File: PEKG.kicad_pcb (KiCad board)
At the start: 2 copper layers, 90 x 45 mm, 78 parts, among them J1 USB_C_Receptacle, J2 AudioJack3, U10 74LVC1G125, U11 74LVC1G125, U12 NCS21802DMR2G, U13 NCS21802DMR2G, U14 NCS21802DMR2G, U5 TS5A63157DBV, U6 TS5A63157DBV, U7 TS5A63157DBV, U8 NCS21802DMR2G, U9 74LVC1G125

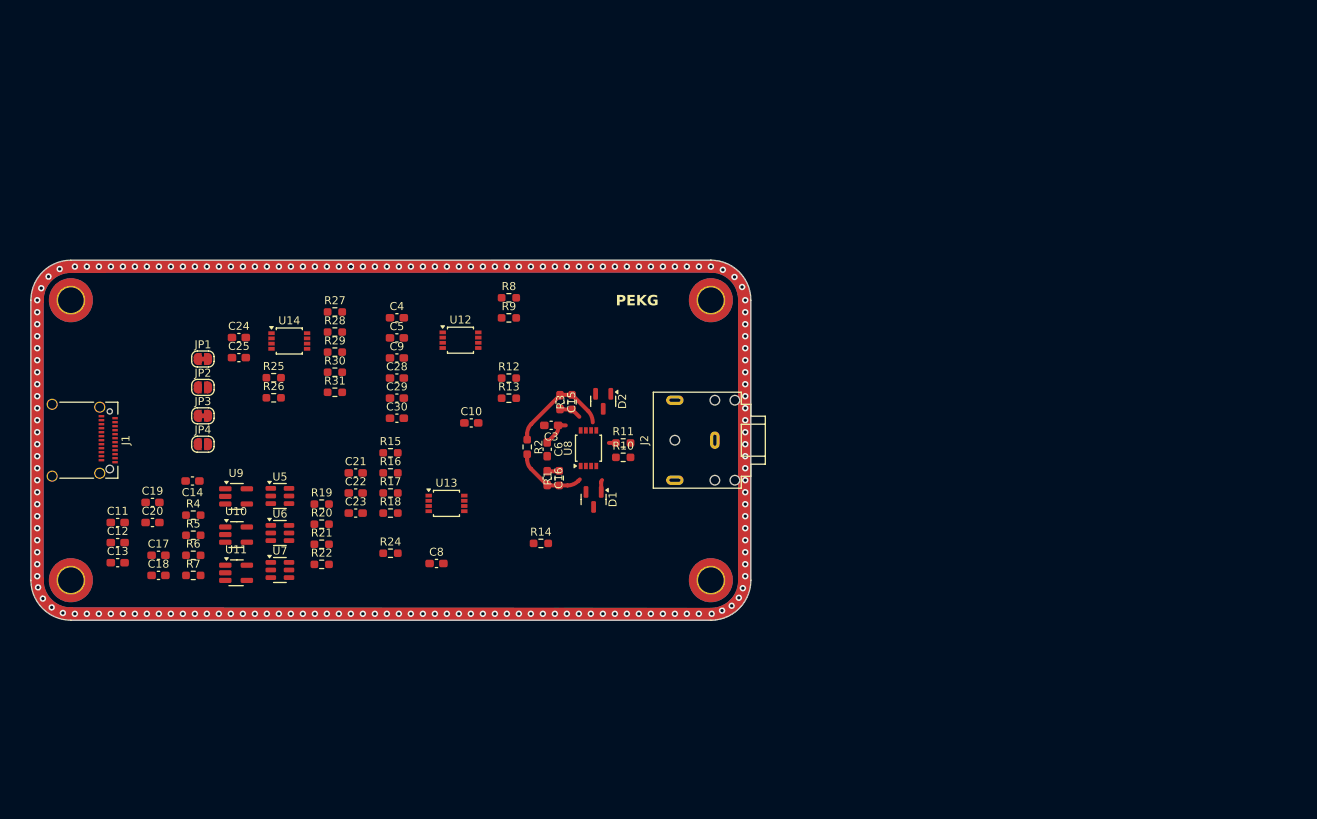
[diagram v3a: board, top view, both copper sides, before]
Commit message: Most all commonents linked to LCSC.
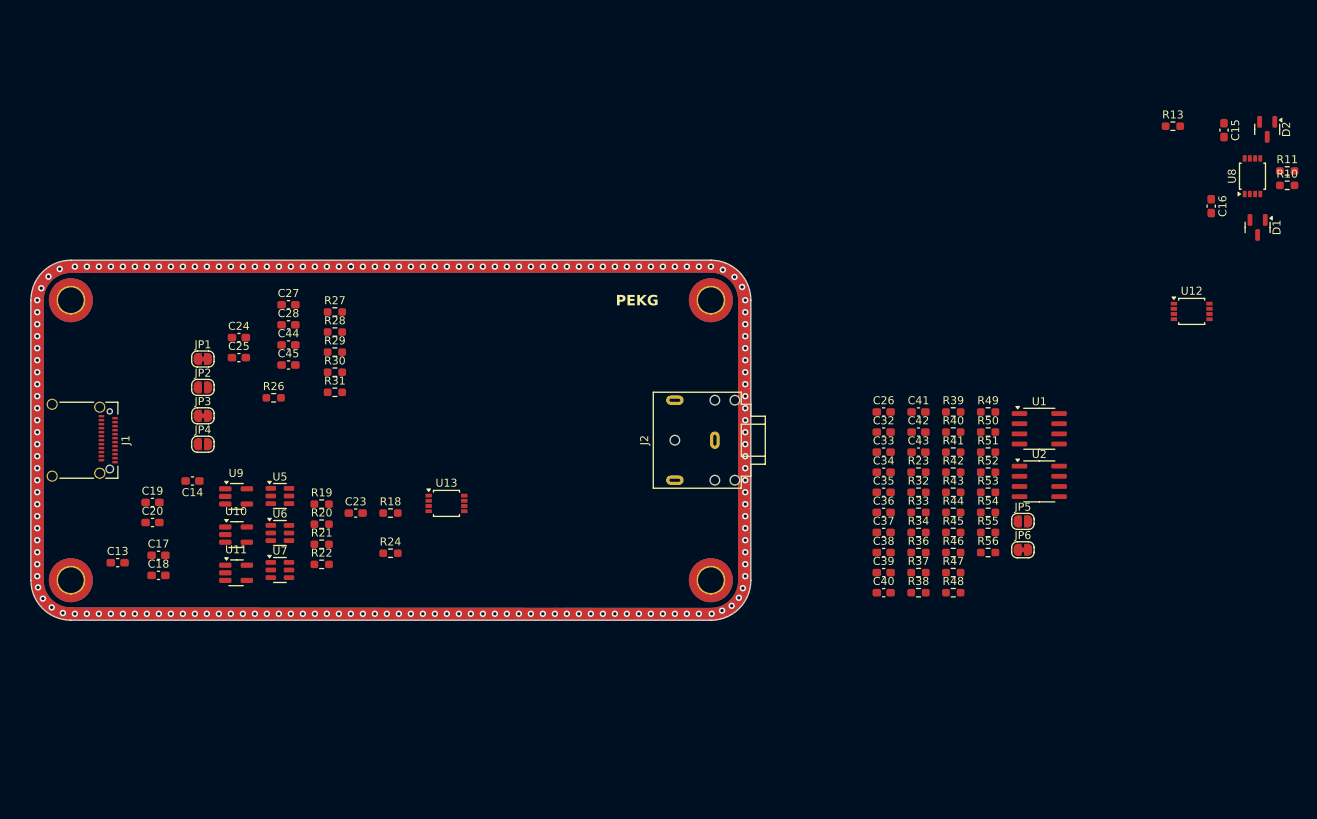
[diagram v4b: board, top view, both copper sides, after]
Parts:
- removed C10, C30, C6, C9: 1u, Capacitor_SMD:C_0603_1608Metric_Pad1.08x0.95mm_HandSolder
- removed C11, C12, C3, C4, C5, C8: 100n, Capacitor_SMD:C_0603_1608Metric_Pad1.08x0.95mm_HandSolder
- removed C21, C22: 10u, Capacitor_SMD:C_0603_1608Metric_Pad1.08x0.95mm_HandSolder
- removed C29: 10n, Capacitor_SMD:C_0603_1608Metric_Pad1.08x0.95mm_HandSolder
- removed R1, R3: 20k, Resistor_SMD:R_0603_1608Metric_Pad0.98x0.95mm_HandSolder
- removed R12, R4, R5, R6, R7: 1k, Resistor_SMD:R_0603_1608Metric_Pad0.98x0.95mm_HandSolder
- removed R14, R15, R16, R17, R25, R8, R9: 100k, Resistor_SMD:R_0603_1608Metric_Pad0.98x0.95mm_HandSolder
- removed R2: 10k, Resistor_SMD:R_0603_1608Metric_Pad0.98x0.95mm_HandSolder
- removed U14: NCS21802DMR2G, Package_SO:OnSemi_Micro8
- added C26: 10u, Capacitor_SMD:C_0603_1608Metric_Pad1.08x0.95mm_HandSolder, F.Cu at (206.6, 119.0)
- added C27: 10u, Capacitor_SMD:C_0603_1608Metric_Pad1.08x0.95mm_HandSolder, F.Cu at (132.2, 105.6)
- added C32: 100n, Capacitor_SMD:C_0603_1608Metric_Pad1.08x0.95mm_HandSolder, F.Cu at (206.6, 121.5)
- added C33: 100n, Capacitor_SMD:C_0603_1608Metric_Pad1.08x0.95mm_HandSolder, F.Cu at (206.6, 124.0)
- added C34: 100n, Capacitor_SMD:C_0603_1608Metric_Pad1.08x0.95mm_HandSolder, F.Cu at (206.6, 126.5)
- added C35: 100n, Capacitor_SMD:C_0603_1608Metric_Pad1.08x0.95mm_HandSolder, F.Cu at (206.6, 129.0)
- added C36: 100n, Capacitor_SMD:C_0603_1608Metric_Pad1.08x0.95mm_HandSolder, F.Cu at (206.6, 131.5)
- added C37: 100n, Capacitor_SMD:C_0603_1608Metric_Pad1.08x0.95mm_HandSolder, F.Cu at (206.6, 134.0)
- added C38: 100n, Capacitor_SMD:C_0603_1608Metric_Pad1.08x0.95mm_HandSolder, F.Cu at (206.6, 136.5)
- added C39: 100n, Capacitor_SMD:C_0603_1608Metric_Pad1.08x0.95mm_HandSolder, F.Cu at (206.6, 139.1)
- added C40: 100n, Capacitor_SMD:C_0603_1608Metric_Pad1.08x0.95mm_HandSolder, F.Cu at (206.6, 141.6)
- added C41: 100n, Capacitor_SMD:C_0603_1608Metric_Pad1.08x0.95mm_HandSolder, F.Cu at (210.9, 119.0)
- added C42: 100n, Capacitor_SMD:C_0603_1608Metric_Pad1.08x0.95mm_HandSolder, F.Cu at (210.9, 121.5)
- added C43: 100n, Capacitor_SMD:C_0603_1608Metric_Pad1.08x0.95mm_HandSolder, F.Cu at (210.9, 124.0)
- added C44: 100n, Capacitor_SMD:C_0603_1608Metric_Pad1.08x0.95mm_HandSolder, F.Cu at (132.2, 110.6)
- added C45: 100n, Capacitor_SMD:C_0603_1608Metric_Pad1.08x0.95mm_HandSolder, F.Cu at (132.2, 113.1)
- added JP5: Jumper_2_Open, Jumper:SolderJumper-2_P1.3mm_Open_RoundedPad1.0x1.5mm, F.Cu at (224.0, 132.7)
- added JP6: Jumper_2_Bridged, Jumper:SolderJumper-2_P1.3mm_Bridged_RoundedPad1.0x1.5mm, F.Cu at (224.0, 136.2)
- added R23: 100k, Resistor_SMD:R_0603_1608Metric_Pad0.98x0.95mm_HandSolder, F.Cu at (210.9, 126.5)
- added R32: 100k, Resistor_SMD:R_0603_1608Metric_Pad0.98x0.95mm_HandSolder, F.Cu at (210.9, 129.0)
- added R33: 10Meg, Resistor_SMD:R_0603_1608Metric_Pad0.98x0.95mm_HandSolder, F.Cu at (210.9, 131.5)
- added R34: 10Meg, Resistor_SMD:R_0603_1608Metric_Pad0.98x0.95mm_HandSolder, F.Cu at (210.9, 134.0)
- added R36: 330k, Resistor_SMD:R_0603_1608Metric_Pad0.98x0.95mm_HandSolder, F.Cu at (210.9, 136.5)
- added R37: 330k, Resistor_SMD:R_0603_1608Metric_Pad0.98x0.95mm_HandSolder, F.Cu at (210.9, 139.1)
- added R38: 330k, Resistor_SMD:R_0603_1608Metric_Pad0.98x0.95mm_HandSolder, F.Cu at (210.9, 141.6)
- added R39: 10Meg, Resistor_SMD:R_0603_1608Metric_Pad0.98x0.95mm_HandSolder, F.Cu at (215.3, 119.0)
- added R40: 330k, Resistor_SMD:R_0603_1608Metric_Pad0.98x0.95mm_HandSolder, F.Cu at (215.3, 121.5)
- added R41: 10k, Resistor_SMD:R_0603_1608Metric_Pad0.98x0.95mm_HandSolder, F.Cu at (215.3, 124.0)
- added R42: 1k, Resistor_SMD:R_0603_1608Metric_Pad0.98x0.95mm_HandSolder, F.Cu at (215.3, 126.5)
- added R43: 1k, Resistor_SMD:R_0603_1608Metric_Pad0.98x0.95mm_HandSolder, F.Cu at (215.3, 129.0)
- added R44: 1k, Resistor_SMD:R_0603_1608Metric_Pad0.98x0.95mm_HandSolder, F.Cu at (215.3, 131.5)
- added R45: 1k, Resistor_SMD:R_0603_1608Metric_Pad0.98x0.95mm_HandSolder, F.Cu at (215.3, 134.0)
- added R46: 1k, Resistor_SMD:R_0603_1608Metric_Pad0.98x0.95mm_HandSolder, F.Cu at (215.3, 136.5)
- added R47: 20k, Resistor_SMD:R_0603_1608Metric_Pad0.98x0.95mm_HandSolder, F.Cu at (215.3, 139.1)
- added R48: 20k, Resistor_SMD:R_0603_1608Metric_Pad0.98x0.95mm_HandSolder, F.Cu at (215.3, 141.6)
- added R49: 20k, Resistor_SMD:R_0603_1608Metric_Pad0.98x0.95mm_HandSolder, F.Cu at (219.7, 119.0)
- added R50: 20k, Resistor_SMD:R_0603_1608Metric_Pad0.98x0.95mm_HandSolder, F.Cu at (219.7, 121.5)
- added R51: 100k, Resistor_SMD:R_0603_1608Metric_Pad0.98x0.95mm_HandSolder, F.Cu at (219.7, 124.0)
- added R52: 100k, Resistor_SMD:R_0603_1608Metric_Pad0.98x0.95mm_HandSolder, F.Cu at (219.7, 126.5)
- added R53: 100k, Resistor_SMD:R_0603_1608Metric_Pad0.98x0.95mm_HandSolder, F.Cu at (219.7, 129.0)
- added R54: 100k, Resistor_SMD:R_0603_1608Metric_Pad0.98x0.95mm_HandSolder, F.Cu at (219.7, 131.5)
- added R55: 100k, Resistor_SMD:R_0603_1608Metric_Pad0.98x0.95mm_HandSolder, F.Cu at (219.7, 134.0)
- added R56: 10Meg, Resistor_SMD:R_0603_1608Metric_Pad0.98x0.95mm_HandSolder, F.Cu at (219.7, 136.5)
- added U1: TL072, Package_SO:SOIC-8_3.9x4.9mm_P1.27mm, F.Cu at (226.1, 121.1)
- added U2: TL072, Package_SO:SOIC-8_3.9x4.9mm_P1.27mm, F.Cu at (226.1, 127.7)
- C13, C15, C16, C17, C18, C19, C20: value 100n -> 10n
- C14: value 1u -> 10u
- C25, C28: value 10n -> 10u
- R10, R11: value 1k -> 10k
- R28, R29: value 20k -> 100k
- moved U12 91.5 mm to (245.1, 106.4)
- moved R10 89.7 mm to (257.0, 90.6)
- moved R11 89.7 mm to (257.0, 88.8)
- moved C15 89.7 mm to (249.1, 83.7)
- moved C16 89.7 mm to (247.5, 93.2)
- moved D1 89.7 mm to (253.3, 95.9)
- moved D2 89.7 mm to (254.5, 83.6)
- moved R13 89.7 mm to (242.8, 83.2)
- moved U8 89.7 mm to (252.7, 89.5)
- moved C28 15.1 mm to (132.2, 108.1)
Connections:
- C13 pad 1: VBUS -> DC_COMPENSATION
- C13 pad 2: GND -> Net-(U12A-+)
- C15 pad 1: Net-(U8B--) -> GAIN_500_OUTPUT
- C15 pad 2: /BOTTOM -> Net-(U12A--)
- C16 pad 1: /TOP -> Net-(JP4-A)
- C16 pad 2: Net-(U8A--) -> Net-(U1A-+)
- C17 pad 1: VBUS -> Net-(C17-Pad1)
- C17 pad 2: GND -> GAIN_5000_OUTPUT
- C18 pad 1: VBUS -> Net-(U1B-+)
- C18 pad 2: GND -> Net-(C17-Pad1)
- C19 pad 1: VBUS -> Net-(U1B--)
- C19 pad 2: GND -> Net-(C19-Pad2)
- C20 pad 1: VBUS -> Net-(U1B--)
- C20 pad 2: GND -> Net-(C19-Pad2)
- C24 pad 1: Net-(JP4-A) -> Net-(JP5-A)
- C24 pad 2: Net-(U14A--) -> Net-(U2A-+)
- C25 pad 1: LEVELED_OUTPUT -> VBUS
- C25 pad 2: Net-(U14B--) -> GND
- C28 pad 1: Net-(U12A-+) -> Net-(U13A--)
- C28 pad 2: DC_COMPENSATION -> Net-(JP2-A)
- R10 pad 1: Net-(U8A-+) -> Net-(U8B--)
- R10 pad 2: LEFT_ARM -> Net-(U8A--)
- R11 pad 1: Net-(U8B-+) -> RIGHT_ARM
- R11 pad 2: RIGHT_ARM -> Net-(U8B-+)
- R18 pad 2: VBUS -> GND
- R20 pad 1: Net-(U4-C) -> VBUS
- R20 pad 2: GND -> Net-(C38-Pad2)
- R21 pad 1: VBUS -> Net-(U4-C)
- R21 pad 2: Net-(C11-Pad1) -> GND
- R24 pad 1: GND -> VBUS
- R26 pad 1: Net-(U14A--) -> 2.5V
- R26 pad 2: 2.5V -> Net-(U1A-+)
- R27 pad 1: LEVELED_OUTPUT -> Net-(U2A-+)
- R27 pad 2: Net-(U14B--) -> Net-(JP5-A)
- R28 pad 1: Net-(U14B--) -> Net-(U12A-+)
- R28 pad 2: VBUS -> DC_COMPENSATION
- R29 pad 1: Net-(U14B--) -> Net-(U12A--)
- R29 pad 2: 2.5V -> GAIN_500_OUTPUT
- R30 pad 1: Net-(U14B-+) -> GAIN_5000_OUTPUT
- R30 pad 2: GAIN_5000_OUTPUT -> Net-(U2A--)
- R31 pad 1: Net-(U14B-+) -> 2.5V
- R31 pad 2: 2.5V -> Net-(U2A--)
- U11 pad 2: Net-(C11-Pad1) -> Net-(C38-Pad2)
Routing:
- net Net-(U8B--): track 13.1 -> 0.00 mm
- net Net-(U8A--): track 9.13 -> 0.00 mm
- net VBUS: track 3.44 -> 0.00 mm
- net /BOTTOM: track 2.82 -> 0.00 mm
- net /TOP: track 1.55 -> 0.00 mm
- net GND: track 1.51 -> 0.00 mm
- net Net-(U8B-+): track 0.88 -> 0.00 mm

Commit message: Inst. amp. added, rough placement done.
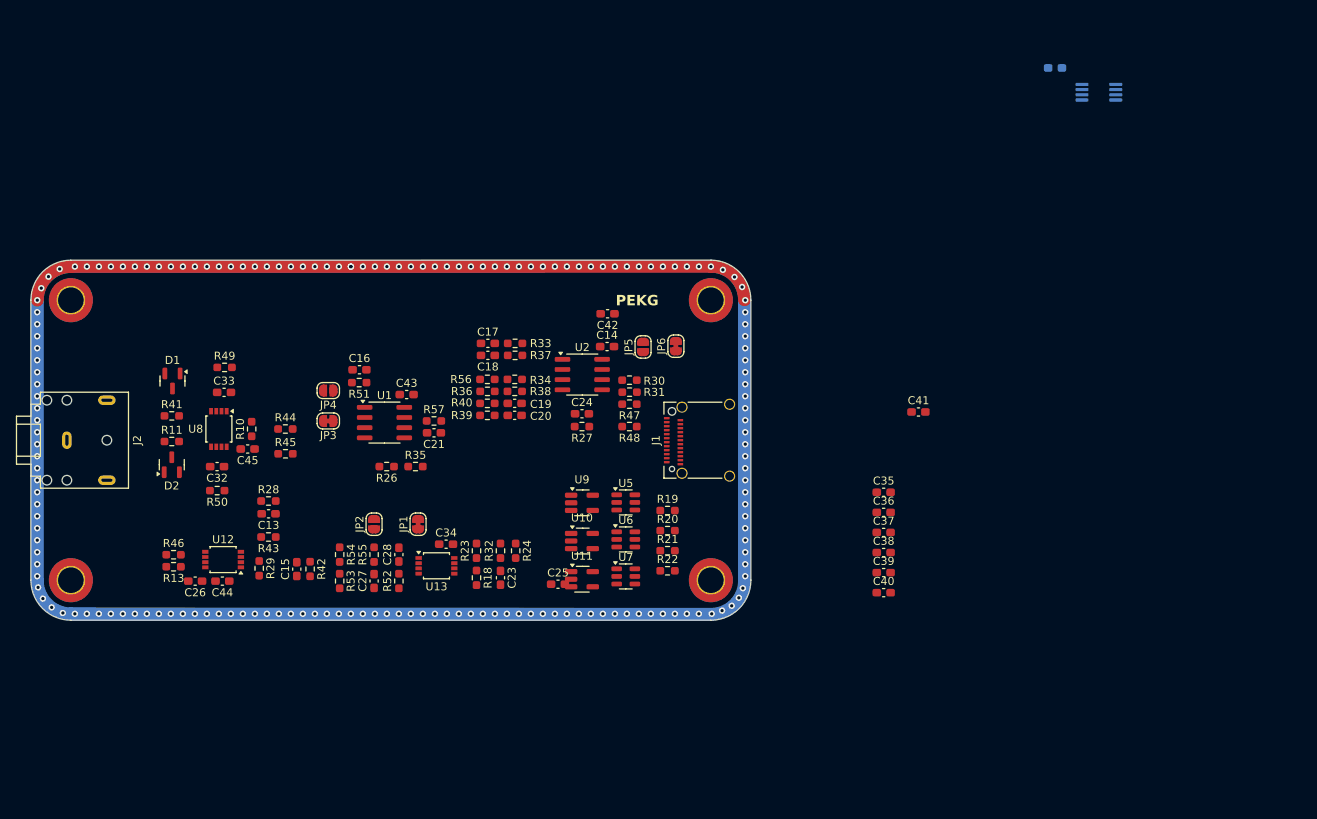
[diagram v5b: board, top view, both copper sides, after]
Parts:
- added C21: 10n, Capacitor_SMD:C_0603_1608Metric_Pad1.08x0.95mm_HandSolder, F.Cu at (150.4, 121.6)
- added C46: 100n, Capacitor_SMD:C_0603_1608Metric_Pad1.08x0.95mm_HandSolder, B.Cu at (228.0, 76.0)
- added R35: 10k, Resistor_SMD:R_0603_1608Metric_Pad0.98x0.95mm_HandSolder, F.Cu at (148.1, 125.8)
- added R57: 100k, Resistor_SMD:R_0603_1608Metric_Pad0.98x0.95mm_HandSolder, F.Cu at (150.4, 120.1)
- added U3: INA350CDSIDDFR, Package_SO:MSOP-8_3x3mm_P0.65mm, B.Cu at (233.5, 79.0)
- moved R11 143.5 mm to (117.6, 122.7)
- moved D2 143.2 mm to (117.6, 125.6), turned to 90 degrees
- moved D1 137.0 mm to (117.7, 115.1)
- moved R13 136.5 mm to (117.8, 138.3), turned to 180 degrees
- moved U8 133.0 mm to (123.5, 121.1), turned to -90 degrees
- moved R10 133.0 mm to (127.6, 121.1), turned to 90 degrees
- moved C15 128.2 mm to (133.2, 138.6), turned to 90 degrees
- moved U12 125.0 mm to (124.0, 137.4), turned to 180 degrees
- moved C16 108.4 mm to (141.1, 113.7), turned to 0 degrees
- moved R41 97.8 mm to (117.6, 119.5)
- moved R46 97.5 mm to (117.8, 136.8)
- moved R50 96.6 mm to (123.3, 128.8), turned to 180 degrees
- moved R49 95.6 mm to (124.2, 113.4)
- moved C26 88.6 mm to (120.5, 140.1), turned to 180 degrees
- moved R43 85.8 mm to (129.7, 134.6), turned to 180 degrees
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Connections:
- net Net-(U8A-+) renamed /LA_IN
- net Net-(U8B-+) renamed /RA_IN
- C18 pad 1: Net-(U1B-+) -> Net-(U2A-+)
- C19 pad 1: Net-(U1B--) -> Net-(U2A--)
- C20 pad 1: Net-(U1B--) -> Net-(U2A--)
- C24 pad 2: Net-(U2A-+) -> Net-(U2B-+)
- R27 pad 1: Net-(U2A-+) -> Net-(U2B-+)
- R30 pad 2: Net-(U2A--) -> Net-(U2B--)
- R31 pad 2: Net-(U2A--) -> Net-(U2B--)
- R34 pad 1: Net-(U1B-+) -> Net-(U2A-+)
- R36 pad 1: Net-(U1B--) -> Net-(U2A--)
- R38 pad 1: Net-(U1B-+) -> Net-(U2A-+)
- R39 pad 1: Net-(U1B--) -> Net-(U2A--)
- R40 pad 1: Net-(U1B--) -> Net-(U2A--)
- R47 pad 2: Net-(U2A-+) -> Net-(U2B-+)
- R48 pad 2: Net-(U2A-+) -> Net-(U2B-+)
- R56 pad 1: Net-(U1B--) -> Net-(U2A--)
- U1 pad 6: Net-(U1B--) -> GAIN_50_OUTPUT
- U1 pad 7: FIL_OUT -> GAIN_500_OUTPUT
- U2 pad 1: Net-(JP5-A) -> FIL_OUT
- U2 pad 5: unconnected-(U2B-+-Pad5) -> Net-(U2B-+)
- U2 pad 6: unconnected-(U2B---Pad6) -> Net-(U2B--)
- U2 pad 7: unconnected-(U2-Pad7) -> Net-(JP5-A)

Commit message: Fixed incorrect filter and gain amp circuits.
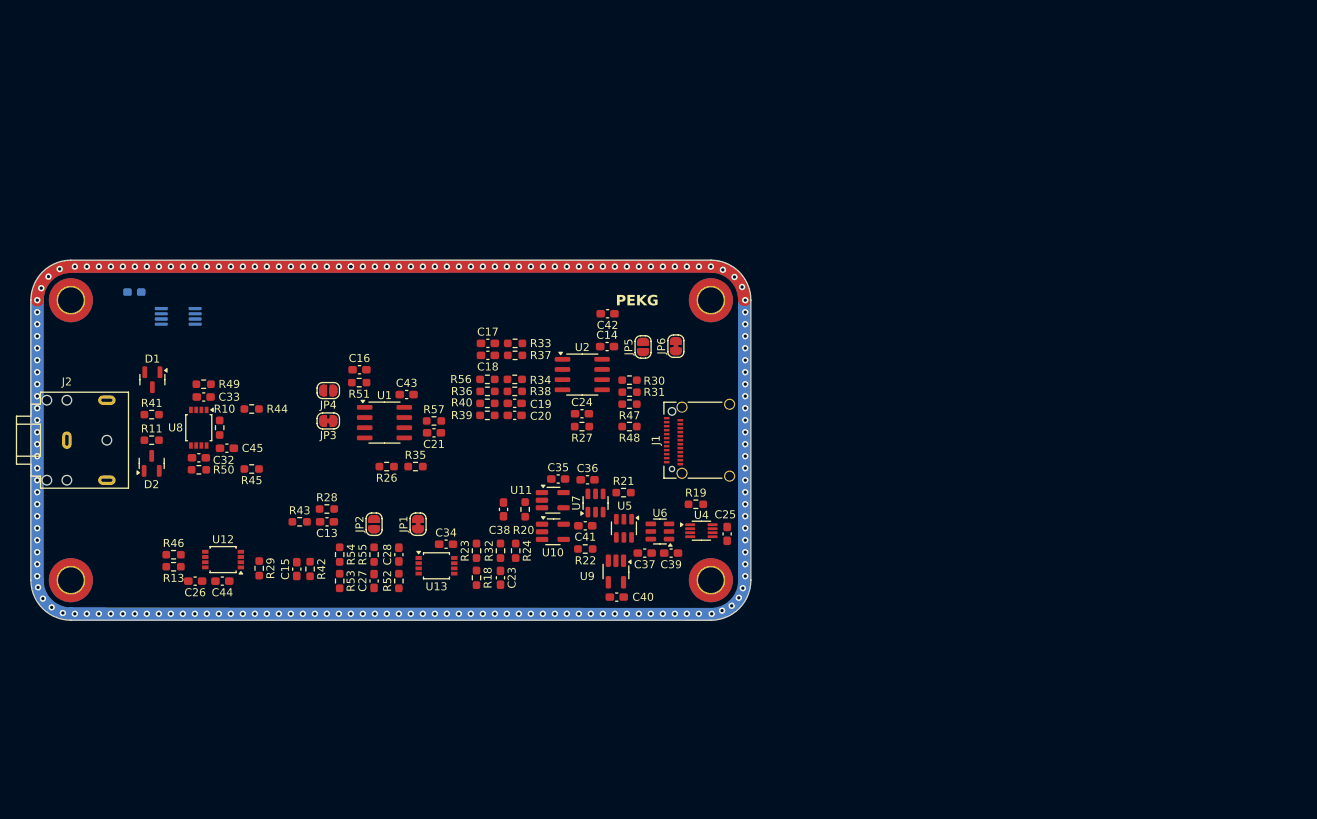
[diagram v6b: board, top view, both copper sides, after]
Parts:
- added U4: 74LVC2G74, Package_SO:VSSOP-8_2.3x2mm_P0.5mm, F.Cu at (183.8, 133.8)
- moved C46 118.5 mm to (112.9, 104.0)
- moved U3 118.5 mm to (118.4, 107.0)
- moved C38 47.8 mm to (159.1, 131.2), turned to 90 degrees
- moved C41 44.0 mm to (169.3, 133.2), turned to 180 degrees
- moved C35 40.7 mm to (165.9, 127.3)
- moved C36 37.2 mm to (169.6, 127.5)
- moved C40 33.4 mm to (173.2, 142.1)
- moved C37 30.0 mm to (176.7, 136.6), turned to 180 degrees
- moved C39 26.7 mm to (180.0, 136.6), turned to 180 degrees
- moved C25 22.1 mm to (187.0, 134.2), turned to -90 degrees
- moved R20 18.0 mm to (161.8, 131.2), turned to 90 degrees
- moved R22 10.6 mm to (169.3, 136.1)
- moved U11 10.5 mm to (165.2, 130.0)
- moved U7 9.93 mm to (170.6, 130.3), turned to 90 degrees
- moved U9 9.58 mm to (173.1, 138.9), turned to -90 degrees
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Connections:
- C21 pad 2: Net-(U1B-+) -> Net-(U1B--)
- R35 pad 2: Net-(U1B-+) -> Net-(U1B--)
- R57 pad 1: Net-(U1B-+) -> Net-(U1B--)
- U1 pad 5: Net-(U1B-+) -> GAIN_50_OUTPUT
- U1 pad 6: GAIN_50_OUTPUT -> Net-(U1B--)
